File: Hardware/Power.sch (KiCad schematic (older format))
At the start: 19 parts, among them U1 TPS63031DSKR, U2 TPS63002

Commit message: Save work from OTH
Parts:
- added TP?: TestPoint, symbol E-Ink:TestPoint
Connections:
- net +5V: now also TP?.1
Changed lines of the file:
@@
 EESchema Schematic File Version 4
-EELAYER 30 0
+LIBS:E-Ink-cache
+EELAYER 29 0
 EELAYER END
 $Descr A4 11693 8268
@@
 	1    0    0    -1
 $EndComp
-Wire Wire Line
-	1600 3600 1800 3600
 Text GLabel 1700 4050 2    50   Output ~ 0
 EN_5V
@@
 	2050 3850 1800 3850
 Connection ~ 1800 3850
+$Comp
+L E-Ink:TestPoint TP?
+U 1 1 5DE5373B
+P 2050 3600
+AR Path="/5DE5A7F7/5DE5373B" Ref="TP?"  Part="1"
+AR Path="/5DE12E8E/5DE5373B" Ref="TP?"  Part="1"
+F 0 "TP?" H 2108 3718 50  0000 L CNN
+F 1 "TestPoint" H 2108 3627 50  0000 L CNN
+F 2 "" H 2250 3600 50  0001 C CNN
+F 3 "~" H 2250 3600 50  0001 C CNN
+	1    2050 3600
+	1    0    0    -1
+$EndComp
+Wire Wire Line
+	1600 3600 1800 3600
+Connection ~ 1800 3600
+Wire Wire Line
+	1800 3600 2050 3600
 $EndSCHEMATC

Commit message: Martin ist unförmig
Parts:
- removed PS1: AAA_Batterypack, symbol E-Ink:AAA_Batterypack
- added Q201: BC847B_215-dk_Transistors-Bipolar-BJT-Single, digikey-footprints:SOT-23-3, symbol E-Ink-rescue:BC847B_215-dk_Transistors-Bipolar-BJT-Single
- added R201: 4k7, Resistor_SMD:R_0805_2012Metric_Pad1.15x1.40mm_HandSolder, symbol E-Ink:4k7
- added R202: 47k, Resistor_SMD:R_0805_2012Metric_Pad1.15x1.40mm_HandSolder, symbol E-Ink:47k
- added R203: 10k, Resistor_SMD:R_0805_2012Metric_Pad1.15x1.40mm_HandSolder, symbol E-Ink:10k
- L201: renamed from L1; footprint (none) -> E-Ink:L_Taiyo-Yuden_MD-3030
- L202: renamed from L2; footprint (none) -> E-Ink:L_Taiyo-Yuden_MD-3030
- TP201, TP202: renamed from TP?; footprint (none) -> digikey-footprints:Test_Point_D1.02mm; Digi-Key_PN (none) -> 36-5001-ND
- U201: renamed from U2; value TPS63002 -> TPS63002DRCR
- U202: renamed from U1; footprint Package_SON:Texas_S-PWSON-N10 -> E-Ink:WSON-8-1EP_3x3mm_P0.5mm_EP1.6x2.0mm
- renumbered C6 to C201, C7 to C202, C1 to C203, C2 to C204, C3 to C205, C8 to C206, C4 to C207, C9 to C208, C5 to C209, C10 to C210, R2 to R204, R1 to R205, R3 to R206
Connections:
- net EN_5V: now also R201.1; no longer U201.6 (EN)
- net GND: now also R203.2
- net at R204.2, U201.8 (VINA): now also Q201.3 (C)
- new net: Q201.2 (E), R202.2, R203.1, U201.6 (EN)
- new net: Q201.1 (B), R201.2, R202.1
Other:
- note removed: "3 * 1.5V AAA Battery -> 4,5V"
- note removed: "EN_5V vllt standartmäßig auf vina legen, und bei nur bei disable mit ESP auf 0V ziehen."
- moved on the sheet: C201, C202, C203, C204, C205, C206, C207, C208, C209, C210, L201, L202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

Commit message: Ich hoffe wir koennen jetzt den Master mergen!
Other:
- note added: "MOSFET statt Bipolar\n"
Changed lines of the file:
@@
 Wire Wire Line
 	6650 4250 7350 4250
+Text Notes 6150 3950 0    20   ~ 4
+MOSFET statt Bipolar\n
 $EndSCHEMATC

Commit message: Zwischenspeicher Arbeit OTH
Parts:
- removed Q201: BC847B_215-dk_Transistors-Bipolar-BJT-Single, digikey-footprints:SOT-23-3, symbol E-Ink-rescue:BC847B_215-dk_Transistors-Bipolar-BJT-Single
- added Q201: 2N7000, digikey-footprints:TO-92-3, symbol E-Ink:2N7000
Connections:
- net at R202.2, R203.1, U201.6 (EN): now also Q201.1 (S)
- net at R204.2, U201.8 (VINA): now also Q201.3 (D)
- net at R201.2, R202.1: now also Q201.2 (G)
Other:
- moved on the sheet: R202
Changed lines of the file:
@@
 EESchema Schematic File Version 4
-EELAYER 30 0
+LIBS:E-Ink-cache
+EELAYER 29 0
 EELAYER END
 $Descr A4 11693 8268
@@
 	4050 3750 6950 3750
 Connection ~ 6950 3750
-$Comp
-L E-Ink-rescue:BC847B_215-dk_Transistors-Bipolar-BJT-Single Q?
-U 1 1 5DF33B75
-P 6300 4350
-AR Path="/5DF33B75" Ref="Q?"  Part="1"
-AR Path="/5DE4BC0A/5DF33B75" Ref="Q?"  Part="1"
-AR Path="/5DE12E8E/5DF33B75" Ref="Q201"  Part="1"
-F 0 "Q201" H 6200 4600 60  0000 C CNN
-F 1 "BC847B_215-dk_Transistors-Bipolar-BJT-Single" H 5950 4500 60  0001 C CNN
-F 2 "digikey-footprints:SOT-23-3" H 6500 4550 60  0001 L CNN
-F 3 "" H 6500 4650 60  0001 L CNN
-F 4 "1727-2921-1-ND" H 6500 4750 60  0001 L CNN "Digi-Key_PN"
-F 5 "BC847B,215" H 6500 4850 60  0001 L CNN "MPN"
-F 6 "Discrete Semiconductor Products" H 6500 4950 60  0001 L CNN "Category"
-F 7 "Transistors - Bipolar (BJT) - Single" H 6500 5050 60  0001 L CNN "Family"
-F 8 "https://assets.nexperia.com/documents/data-sheet/BC847_SER.pdf" H 6500 5150 60  0001 L CNN "DK_Datasheet_Link"
-F 9 "/product-detail/en/nexperia-usa-inc/BC847B,215/1727-2921-1-ND/763460" H 6500 5250 60  0001 L CNN "DK_Detail_Page"
-F 10 "TRANS NPN 45V 0.1A SOT23" H 6500 5350 60  0001 L CNN "Description"
-F 11 "Nexperia USA Inc." H 6500 5450 60  0001 L CNN "Manufacturer"
-F 12 "Active" H 6500 5550 60  0001 L CNN "Status"
-	1    6300 4350
-	1    0    0    -1
-$EndComp
 Wire Wire Line
 	6400 4150 6950 4150
@@
 	0    1    1    0
 $EndComp
-Wire Wire Line
-	6650 4750 6400 4750
 $Comp
 L power:GND #PWR?
@@
 L E-Ink:47k R?
 U 1 1 5DF5350A
-P 6100 4700
+P 5800 4700
 AR Path="/5DF5350A" Ref="R?"  Part="1"
 AR Path="/5DE4BC0A/5DF5350A" Ref="R?"  Part="1"
 AR Path="/5DE12E8E/5DF5350A" Ref="R202"  Part="1"
-F 0 "R202" H 6100 4750 50  0000 L CNN
-F 1 "47k" H 6250 4750 50  0000 L CNN
-F 2 "Resistor_SMD:R_0805_2012Metric_Pad1.15x1.40mm_HandSolder" H 6150 4550 50  0001 C CNN
-F 3 "" H 6100 4750 50  0001 C CNN
-	1    6100 4700
+F 0 "R202" H 5700 4750 50  0000 L CNN
+F 1 "47k" H 5950 4750 50  0000 L CNN
+F 2 "Resistor_SMD:R_0805_2012Metric_Pad1.15x1.40mm_HandSolder" H 5850 4550 50  0001 C CNN
+F 3 "" H 5800 4750 50  0001 C CNN
+	1    5800 4700
 	1    0    0    -1
 $EndComp
@@
 	1    0    0    -1
 $EndComp
-Wire Wire Line
-	5700 4350 6000 4350
-Wire Wire Line
-	6000 4750 6000 4350
-Connection ~ 6000 4350
-Wire Wire Line
-	6000 4350 6100 4350
 Connection ~ 6400 4750
 Wire Wire Line
-	6650 4250 6650 4750
-Wire Wire Line
-	6650 4250 7350 4250
+	6900 4250 6900 4750
 Text Notes 6150 3950 0    20   ~ 4
 MOSFET statt Bipolar\n
+$Comp
+L E-Ink:2N7000 Q201
+U 1 1 5DF2F28C
+P 6400 4350
+F 0 "Q201" H 6508 4403 60  0000 L CNN
+F 1 "2N7000" H 6508 4297 60  0000 L CNN
+F 2 "digikey-footprints:TO-92-3" H 6600 4550 60  0001 L CNN
+F 3 "https://www.onsemi.com/pub/Collateral/NDS7002A-D.PDF" H 6600 4650 60  0001 L CNN
+F 4 "2N7000FS-ND" H 6600 4750 60  0001 L CNN "Digi-Key_PN"
+F 5 "2N7000" H 6600 4850 60  0001 L CNN "MPN"
+F 6 "Discrete Semiconductor Products" H 6600 4950 60  0001 L CNN "Category"
+F 7 "Transistors - FETs, MOSFETs - Single" H 6600 5050 60  0001 L CNN "Family"
+F 8 "https://www.onsemi.com/pub/Collateral/NDS7002A-D.PDF" H 6600 5150 60  0001 L CNN "DK_Datasheet_Link"
+F 9 "/product-detail/en/on-semiconductor/2N7000/2N7000FS-ND/244278" H 6600 5250 60  0001 L CNN "DK_Detail_Page"
+F 10 "MOSFET N-CH 60V 200MA TO-92" H 6600 5350 60  0001 L CNN "Description"
+F 11 "ON Semiconductor" H 6600 5450 60  0001 L CNN "Manufacturer"
+F 12 "Active" H 6600 5550 60  0001 L CNN "Status"
+	1    6400 4350
+	1    0    0    -1
+$EndComp
+Wire Wire Line
+	6100 4750 6400 4750
+Wire Wire Line
+	5700 4750 5700 4350
+Wire Wire Line
+	6100 4450 6100 4350
+Wire Wire Line
+	6100 4350 5700 4350
+Connection ~ 5700 4350
+Wire Wire Line
+	6900 4250 7350 4250
+Wire Wire Line
+	6400 4750 6900 4750
 $EndSCHEMATC

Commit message: save work at arges, finished layout and routing
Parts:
- Q201: footprint digikey-footprints:TO-92-3 -> Digikey:TO-92-3
- TP201, TP202: footprint digikey-footprints:Test_Point_D1.02mm -> Digikey:Test_Point_D1.02mm
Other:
- note added: "Footprint für Handsoldering überarbeiten"

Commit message: savecommit
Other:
- note removed: "Footprint für Handsoldering überarbeiten"
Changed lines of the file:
@@
 EESchema Schematic File Version 4
-LIBS:E-Ink-cache
 EELAYER 30 0
 EELAYER END
@@
 Wire Wire Line
 	6400 4750 6900 4750
-Text Notes 7250 1000 0    50   ~ 0
-Footprint für Handsoldering überarbeiten
 Wire Wire Line
 	8450 1250 7350 1250

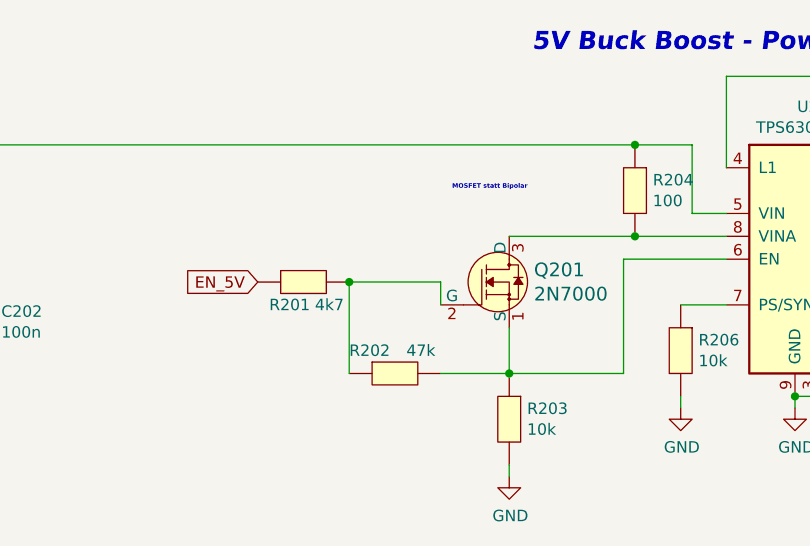
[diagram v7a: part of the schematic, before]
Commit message: Added new MCU and redesigned schematics
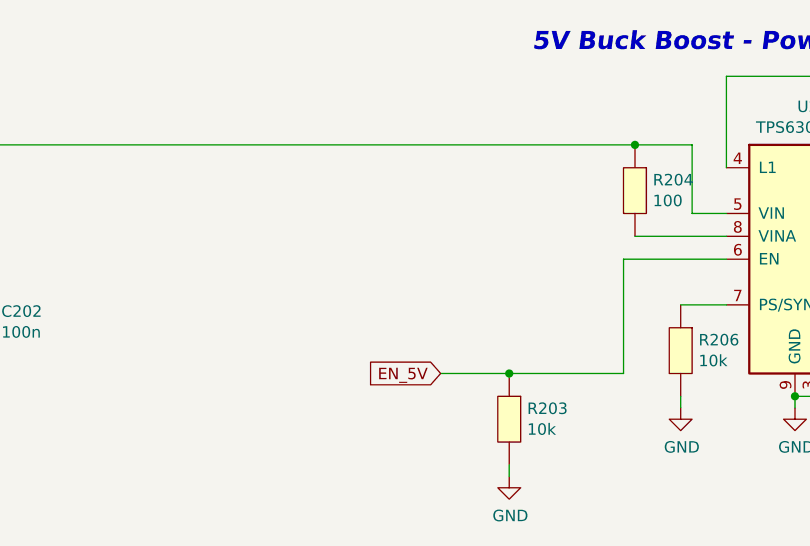
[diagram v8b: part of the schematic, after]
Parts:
- removed Q201: 2N7000, Digikey:TO-92-3, symbol E-Ink:2N7000
- removed R201: 4k7, Resistor_SMD:R_0805_2012Metric_Pad1.15x1.40mm_HandSolder, symbol E-Ink:4k7
- removed R202: 47k, Resistor_SMD:R_0805_2012Metric_Pad1.15x1.40mm_HandSolder, symbol E-Ink:47k
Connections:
- net EN_5V: now also R203.1, U201.6 (EN)
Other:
- note removed: "MOSFET statt Bipolar\n"
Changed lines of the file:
@@
 EESchema Schematic File Version 4
-LIBS:E-Ink-cache
 EELAYER 30 0
 EELAYER END
@@
 Wire Wire Line
 	7150 4450 7350 4450
-Text GLabel 5300 4350 0    50   Input ~ 0
+Text GLabel 6100 4750 0    50   Input ~ 0
 EN_5V
 $Comp
@@
 	4050 3750 6950 3750
 Connection ~ 6950 3750
-Wire Wire Line
-	6400 4150 6950 4150
-Connection ~ 6950 4150
 $Comp
 L E-Ink:10k R?
@@
 Wire Wire Line
 	6400 5150 6400 5200
-$Comp
-L E-Ink:47k R?
-U 1 1 5DF5350A
-P 5800 4700
-AR Path="/5DF5350A" Ref="R?"  Part="1"
-AR Path="/5DE4BC0A/5DF5350A" Ref="R?"  Part="1"
-AR Path="/5DE12E8E/5DF5350A" Ref="R202"  Part="1"
-F 0 "R202" H 5700 4750 50  0000 L CNN
-F 1 "47k" H 5950 4750 50  0000 L CNN
-F 2 "Resistor_SMD:R_0805_2012Metric_Pad1.15x1.40mm_HandSolder" H 5850 4550 50  0001 C CNN
-F 3 "" H 5800 4750 50  0001 C CNN
-	1    5800 4700
-	1    0    0    -1
-$EndComp
-Wire Wire Line
-	6400 4750 6400 4550
-$Comp
-L E-Ink:4k7 R?
-U 1 1 5DF58F68
-P 5400 4300
-AR Path="/5DF58F68" Ref="R?"  Part="1"
-AR Path="/5DE4BC0A/5DF58F68" Ref="R?"  Part="1"
-AR Path="/5DE12E8E/5DF58F68" Ref="R201"  Part="1"
-F 0 "R201" H 5350 4150 50  0000 L CNN
-F 1 "4k7" H 5550 4150 50  0000 L CNN
-F 2 "Resistor_SMD:R_0805_2012Metric_Pad1.15x1.40mm_HandSolder" H 5450 4150 50  0001 C CNN
-F 3 "" H 5400 4350 50  0001 C CNN
-	1    5400 4300
-	1    0    0    -1
-$EndComp
 Connection ~ 6400 4750
 Wire Wire Line
 	6900 4250 6900 4750
-Text Notes 6150 3950 0    20   ~ 4
-MOSFET statt Bipolar\n
-$Comp
-L E-Ink:2N7000 Q201
-U 1 1 5DF2F28C
-P 6400 4350
-F 0 "Q201" H 6508 4403 60  0000 L CNN
-F 1 "2N7000" H 6508 4297 60  0000 L CNN
-F 2 "Digikey:TO-92-3" H 6600 4550 60  0001 L CNN
-F 3 "https://www.onsemi.com/pub/Collateral/NDS7002A-D.PDF" H 6600 4650 60  0001 L CNN
-F 4 "2N7000FS-ND" H 6600 4750 60  0001 L CNN "Digi-Key_PN"
-F 5 "2N7000" H 6600 4850 60  0001 L CNN "MPN"
-F 6 "Discrete Semiconductor Products" H 6600 4950 60  0001 L CNN "Category"
-F 7 "Transistors - FETs, MOSFETs - Single" H 6600 5050 60  0001 L CNN "Family"
-F 8 "https://www.onsemi.com/pub/Collateral/NDS7002A-D.PDF" H 6600 5150 60  0001 L CNN "DK_Datasheet_Link"
-F 9 "/product-detail/en/on-semiconductor/2N7000/2N7000FS-ND/244278" H 6600 5250 60  0001 L CNN "DK_Detail_Page"
-F 10 "MOSFET N-CH 60V 200MA TO-92" H 6600 5350 60  0001 L CNN "Description"
-F 11 "ON Semiconductor" H 6600 5450 60  0001 L CNN "Manufacturer"
-F 12 "Active" H 6600 5550 60  0001 L CNN "Status"
-	1    6400 4350
-	1    0    0    -1
-$EndComp
 Wire Wire Line
 	6100 4750 6400 4750
 Wire Wire Line
-	5700 4750 5700 4350
-Wire Wire Line
-	6100 4450 6100 4350
-Wire Wire Line
-	6100 4350 5700 4350
-Connection ~ 5700 4350
-Wire Wire Line
 	6900 4250 7350 4250
